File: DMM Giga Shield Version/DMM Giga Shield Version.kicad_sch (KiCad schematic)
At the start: 81 parts, among them J1 Conn_01x07_Pin, J10 ANALOG, J11 I_Input, J12 Conn_01x02_Pin, J13 DIGITAL1, J14 Barrel_Jack, J15 Barrel_Jack, J16 Conn_01x01_Socket, J17 Conn_01x01_Socket, J2 MicoSD, J3 Conn_01x07_Pin, J5 POWER2, J6 POWER1, J7 Conn_01x02_Pin, J8 DIGITAL2, J9 Out to Screen, Q1 MMBT3904, Q2 AO3400A MOSFET, Q6 BSS138, Q7 BSS138, Q8 AO3400A MOSFET, SW1 SW_Push, SW2 SW_Push, SW3 SW_SPDT, SW4 SW_Push, U1 LM317_TO-220, U10 LM4040DBZ-2.5, U11 LM4040DBZ-5, U12 TLV61046ADBVR, U2 IX4426N, U3 ADS1115IDGS, U4 IX4426N, U5 Opamp_Dual, U7 MAX1683, U8 Opamp_Dual, U9 TPS613222ADBV

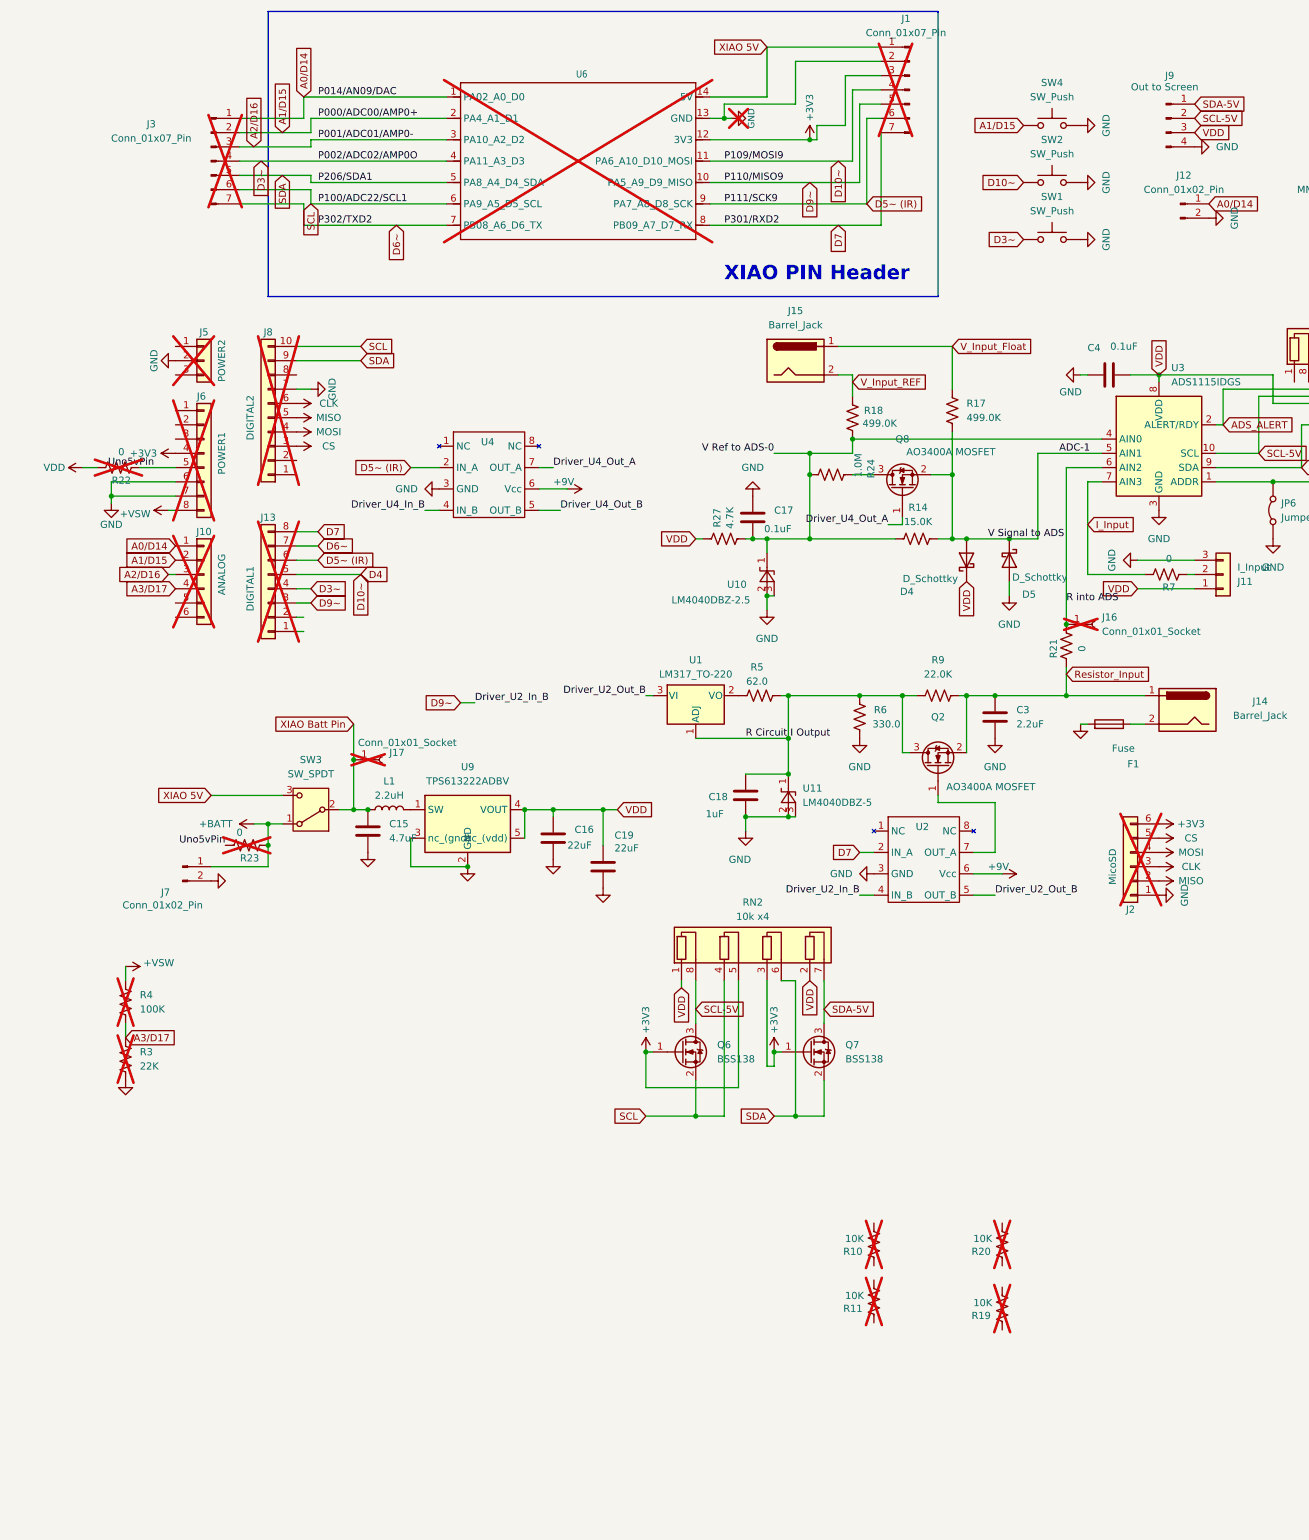
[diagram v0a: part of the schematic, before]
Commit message: Working on PCBs and Separating Out Different Versions
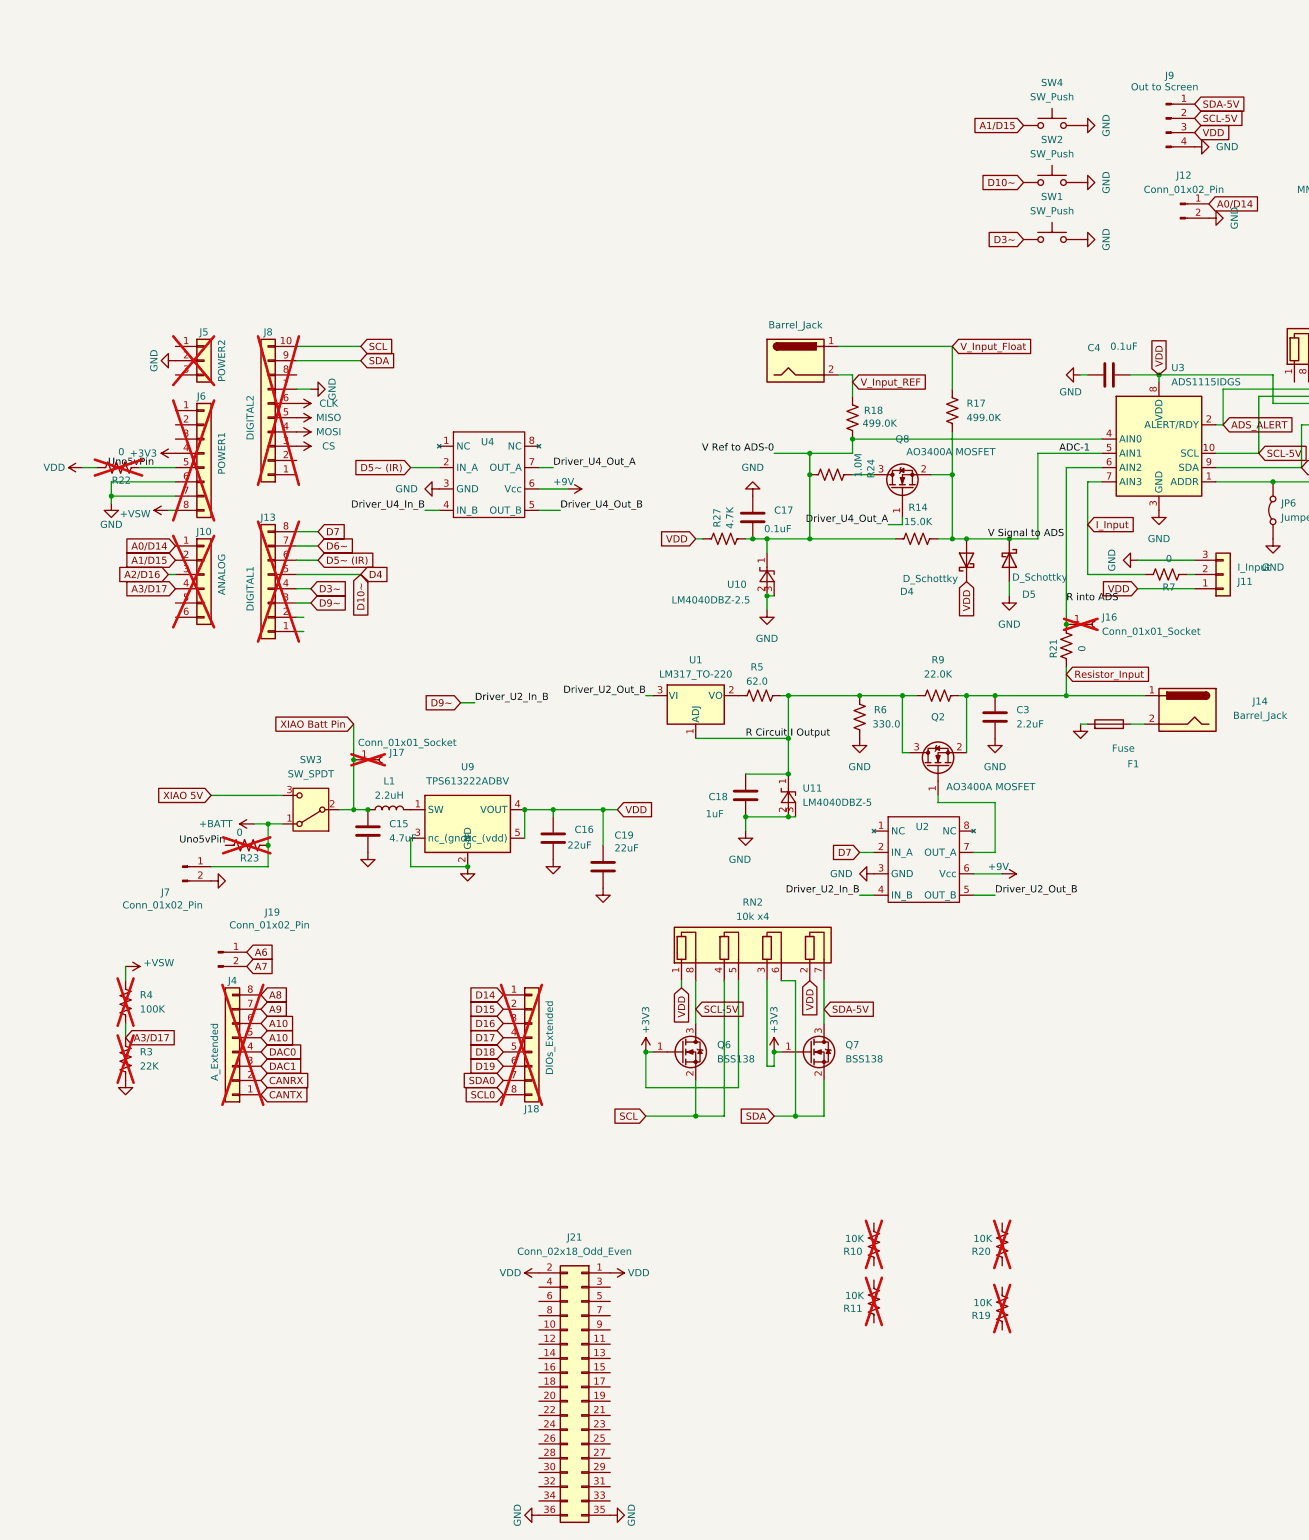
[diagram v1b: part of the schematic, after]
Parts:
- removed J1, J3: Conn_01x07_Pin, Connector_PinSocket_2.54mm:PinSocket_1x07_P2.54mm_Vertical, symbol Connector:Conn_01x07_Pin
- removed J2: MicoSD, Connector_PinSocket_2.54mm:PinSocket_1x06_P2.54mm_Vertical, symbol Connector_Generic:Conn_01x06
- removed U6: ~, symbol Seeed_libdb:Module/XIAO-HALF-HOLE
- added J18: DIOs_Extended, Connector_PinHeader_2.54mm:PinHeader_1x08_P2.54mm_Vertical, symbol Connector_Generic:Conn_01x08
- added J19: Conn_01x02_Pin, Connector_PinSocket_2.54mm:PinSocket_1x02_P2.54mm_Vertical, symbol Connector:Conn_01x02_Pin
- added J21: Conn_02x18_Odd_Even, Connector_PinSocket_2.54mm:PinSocket_2x18_P2.54mm_Vertical, symbol Connector_Generic:Conn_02x18_Odd_Even
- added J4: A_Extended, Connector_PinHeader_2.54mm:PinHeader_1x08_P2.54mm_Vertical, symbol Connector_Generic:Conn_01x08
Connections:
- net GND: now also J21.35 (Pin_35), J21.36 (Pin_36)
- net VDD: now also J21.1 (Pin_1), J21.2 (Pin_2)
- new net A10: J4.5 (Pin_5), J4.6 (Pin_6)
- new net A6: J19.1 (Pin_1)
- new net A7: J19.2 (Pin_2)
- new net A8: J4.8 (Pin_8)
- new net A9: J4.7 (Pin_7)
- new net CANRX: J4.2 (Pin_2)
- new net CANTX: J4.1 (Pin_1)
- new net D14: J18.1 (Pin_1)
- new net D15: J18.2 (Pin_2)
- new net D16: J18.3 (Pin_3)
- new net D17: J18.4 (Pin_4)
- new net D18: J18.5 (Pin_5)
- new net D19: J18.6 (Pin_6)
- new net DAC0: J4.4 (Pin_4)
- new net DAC1: J4.3 (Pin_3)
- new net SCL0: J18.8 (Pin_8)
- new net SDA0: J18.7 (Pin_7)
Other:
- note removed: "XIAO PIN Header"

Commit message: Consolidated Data Sheets for used (or might use) components), PCB edits.
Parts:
- added J1: TRRS, Connector_PinSocket_2.54mm:PinSocket_1x04_P2.54mm_Vertical, symbol Connector:Conn_01x04_Pin
- U5: now fitted
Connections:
- net DAC1: now also U5.3 (+)
- net GND: now also U5.4 (V-), J1.3 (Pin_3)
- net VDD: now also U5.8 (V+)
- net at U5.1: now also U5.2 (-)
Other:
- moved on the sheet: C18, D1, J18, JP6, Q1, Q6, Q7, R1, R2, RN1, RN2, U11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
